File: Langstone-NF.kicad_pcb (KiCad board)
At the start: 2 copper layers, 34 parts, among them J1 VCC, J2 Mic_2, J3 Mic_1, J4 AF_Out, J5 AF_In, J6 SP_1, J7 SP_2, U1 LM386, U2 LM386N

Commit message: Using the github plugin
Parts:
- RV1: renamed from RV2; footprint Potentiometer_THT:Potentiometer_ACP_CA9-V10_Vertical -> DF9RY:Potentiometer_ACP_CA6-V10_Vertical
- RV2: renamed from RV1; footprint Potentiometer_THT:Potentiometer_ACP_CA9-V10_Vertical -> DF9RY:Potentiometer_ACP_CA6-V10_Vertical
- renumbered R5 to R4, R6 to R5, R7 to R6, R8 to R7, R9 to R8, R10 to R9

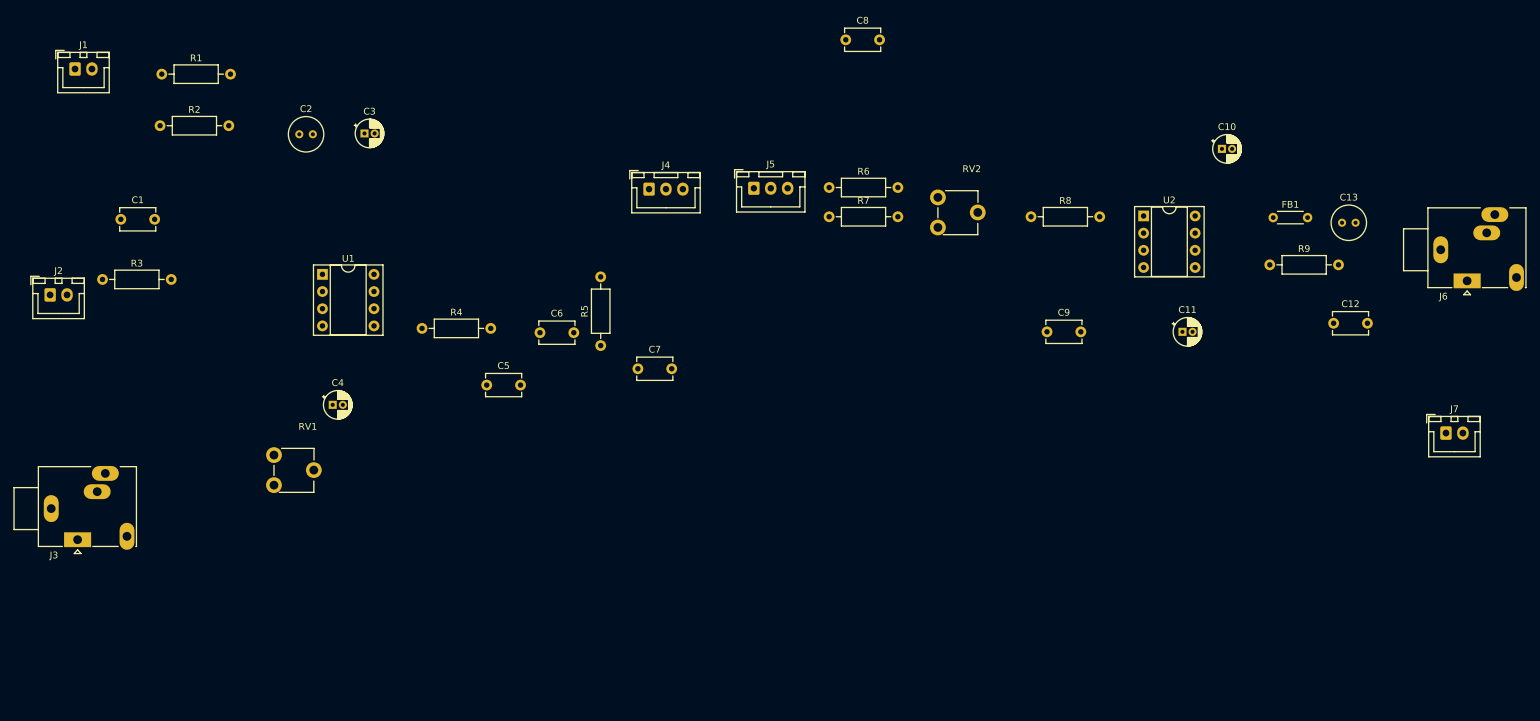
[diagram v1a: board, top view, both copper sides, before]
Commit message: Platinenlayout modifiziert Serie1
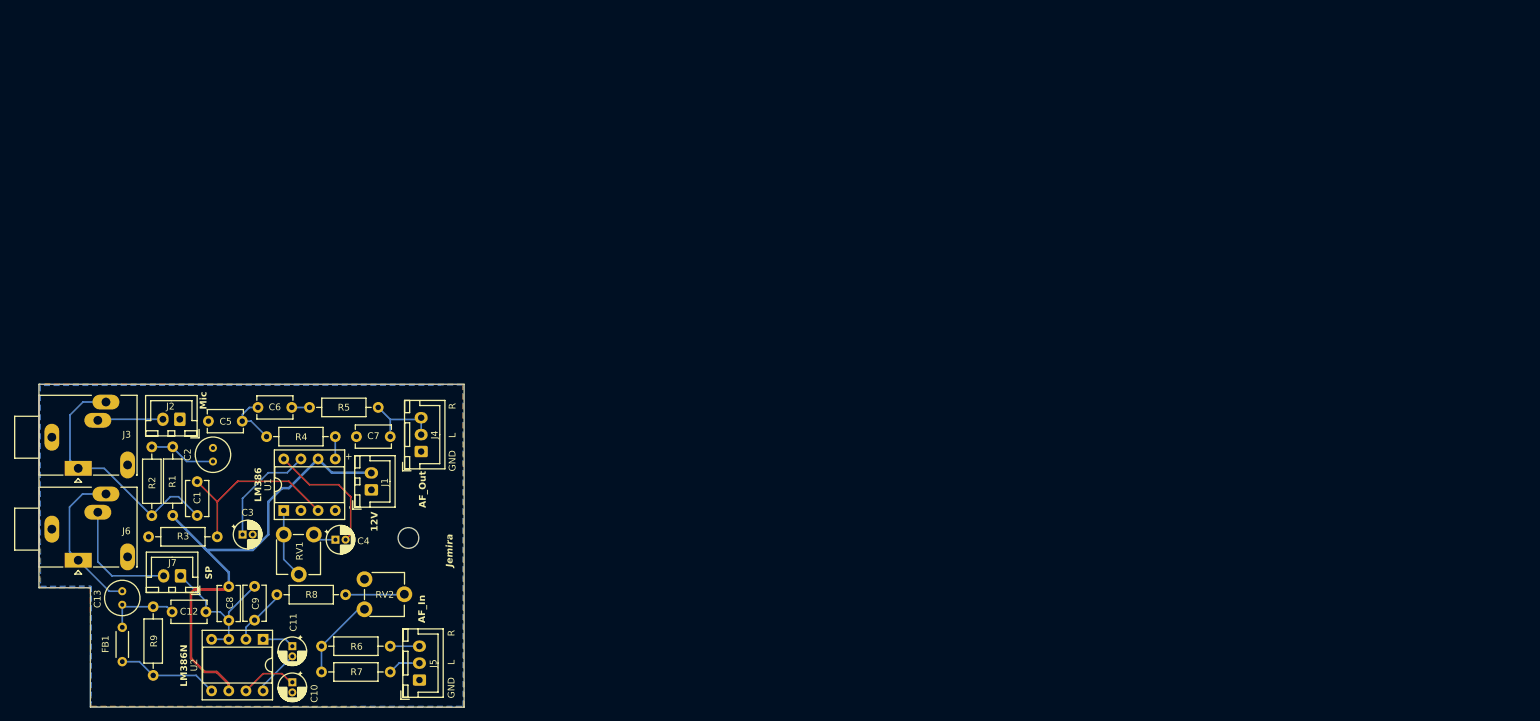
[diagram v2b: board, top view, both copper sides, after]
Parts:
- moved J6 209.5 mm to (62.8, 139.4)
- moved C13 189.0 mm to (69.3, 146.0), turned to 90 degrees
- moved J7 188.3 mm to (78.0, 141.7), turned to 180 degrees
- moved FB1 182.4 mm to (69.3, 154.4), turned to 90 degrees
- moved C12 177.0 mm to (76.7, 147.1)
- moved R9 175.9 mm to (73.9, 156.5), turned to 90 degrees
- moved C10 158.5 mm to (94.5, 157.5), turned to -90 degrees
- moved U2 144.5 mm to (90.2, 151.1), turned to -90 degrees
- moved C11 139.6 mm to (94.5, 152.1), turned to -90 degrees
- moved C8 125.3 mm to (85.1, 148.3), turned to 90 degrees
- moved C9 123.1 mm to (88.9, 143.3), turned to -90 degrees
- moved R8 115.7 mm to (102.4, 144.5), turned to 180 degrees
- moved RV2 101.9 mm to (105.2, 146.7)
- moved R6 93.9 mm to (109.0, 152.1), turned to 180 degrees
- moved R7 93.5 mm to (109.0, 156.0), turned to 180 degrees
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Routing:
- net +12V: track 0.00 -> 71.1 mm
- net Net-(C1-Pad1): track 0.00 -> 37.3 mm
- net Net-(U1-+): track 0.00 -> 27.3 mm
- net Net-(C13-Pad2): track 0.00 -> 23.0 mm
- net GND: track 0.00 -> 22.7 mm
- net Net-(C4-Pad2): track 0.00 -> 18.9 mm
- net Net-(J7-Pin_2): track 0.00 -> 17.9 mm
- net Net-(U1-BYPASS): track 0.00 -> 16.4 mm
- net Net-(FB1-Pad1): track 0.00 -> 15.0 mm
- net Net-(J4-Pin_2): track 0.00 -> 11.9 mm
- net Net-(R6-Pad2): track 0.00 -> 11.5 mm
- net Net-(C12-Pad1): track 0.00 -> 10.7 mm
- net Net-(RV1-Pad1): track 0.00 -> 10.4 mm
- net Net-(C2-Pad1): track 0.00 -> 9.98 mm
- net Net-(J2-Pin_2): track 0.00 -> 9.47 mm
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- added copper zone on B.Cu, net GND
- added copper zone on F.Cu, net GND
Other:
- board outline added: 62.9 x 47.8 mm
- board text added: "+"
- board text added: "-"
- board text added: "12V"
- board text added: "AF_In"
- board text added: "AF_Out"
- board text added: "GND"
- board text added: "Jemira"
- board text added: "L"
- board text added: "LM386"
- board text added: "LM386N"
- board text added: "Mic"
- board text added: "R"
- board text added: "SP"

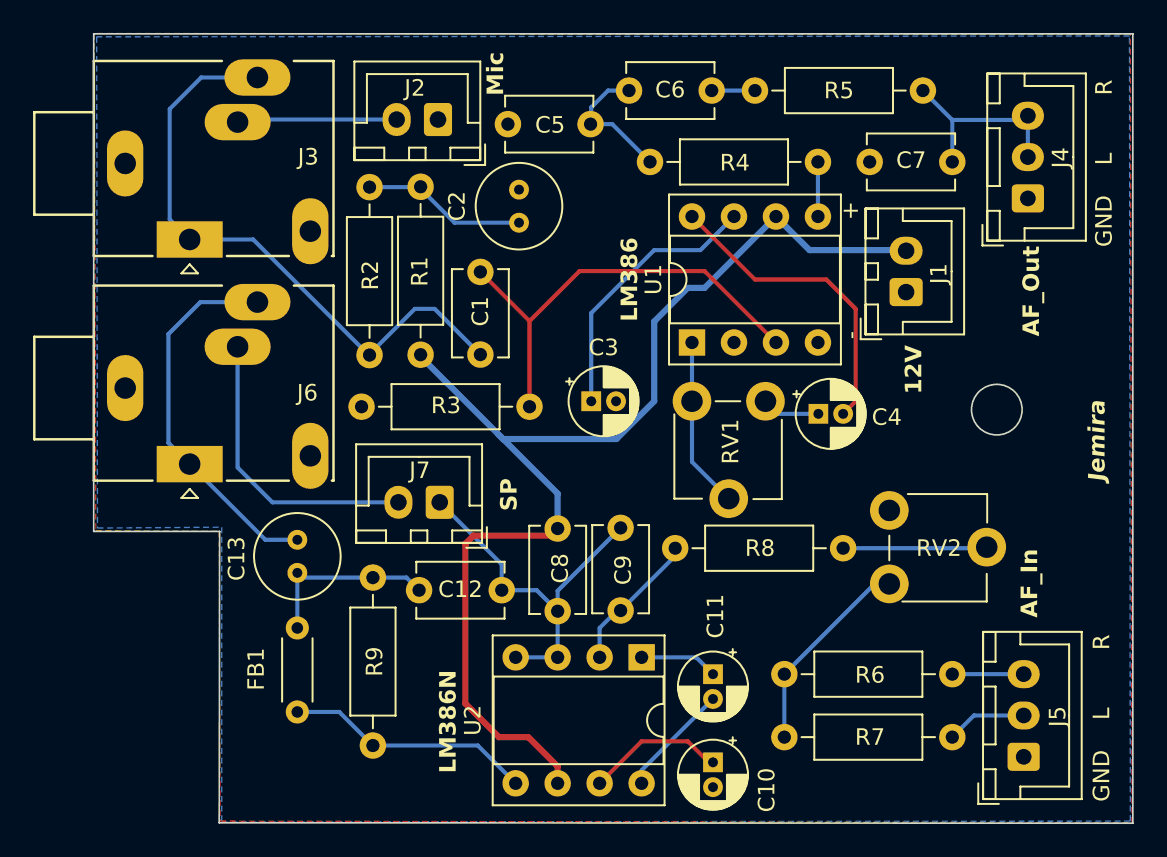
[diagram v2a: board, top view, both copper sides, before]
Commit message: Jemira's Lautsprecherbuchsen Footprints
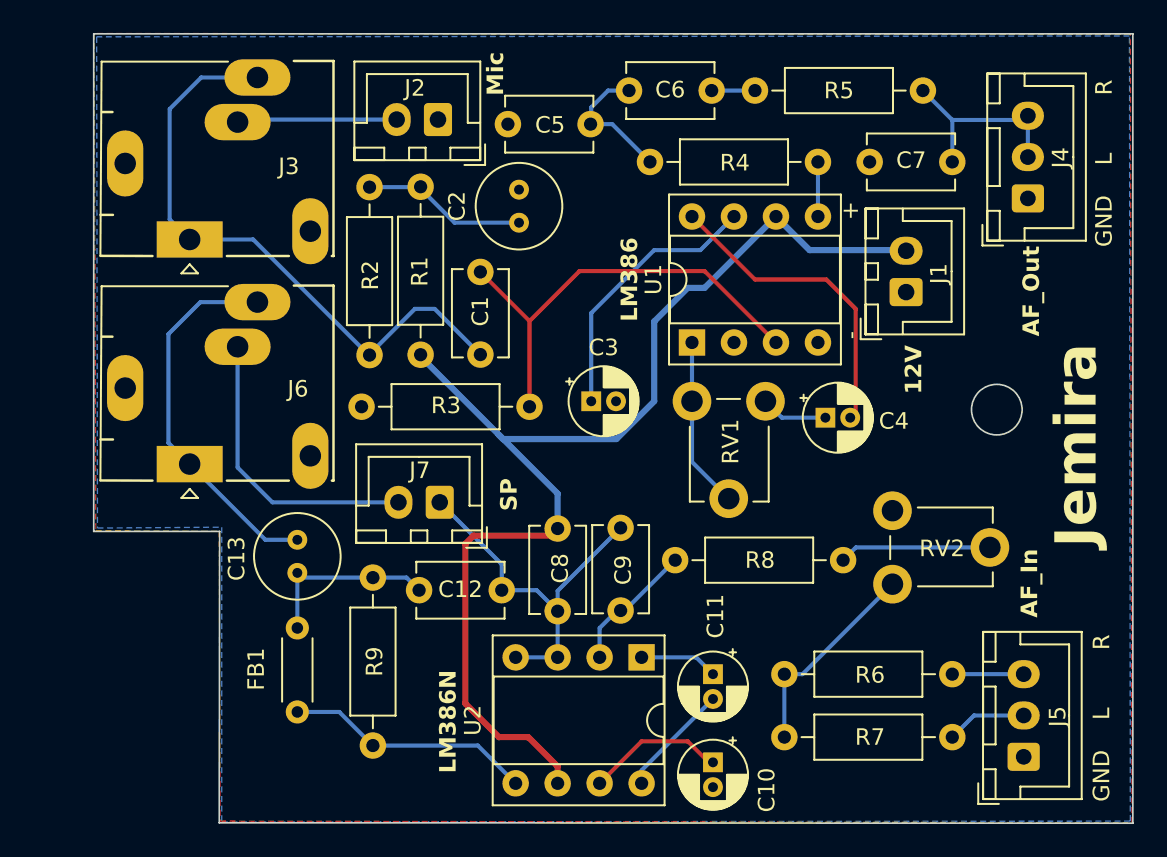
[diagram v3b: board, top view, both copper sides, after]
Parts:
- J3, J6: footprint DF9RY:Jack_3.5mm_Ledino_Stereo_Switch_Horizontal -> DF9RY:Jack_3.5mm_Ledino_Stereo_Switch_Horizontal_Special_Out
- moved R8 0.72 mm to (102.4, 145.2)
- moved C4 0.49 mm to (101.3, 136.6)
- moved RV2 0.19 mm to (105.3, 146.7)
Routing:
- net Net-(R6-Pad2): track 11.5 -> 12.6 mm
- net Net-(R8-Pad1): track 8.62 -> 9.20 mm
- net Net-(C4-Pad1): track 3.51 -> 4.04 mm
